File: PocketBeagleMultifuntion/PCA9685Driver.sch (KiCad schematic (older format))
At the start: 18 parts, among them P601 A7 A6 A5 A4 A3 A2 A1 A0 C, P602 B7 B6 B5 B4 B3 B2 B1 B0 C, T601 + 12V -, U601 PCA9685, U602 TBD62X83A, U603 TBD62X83A

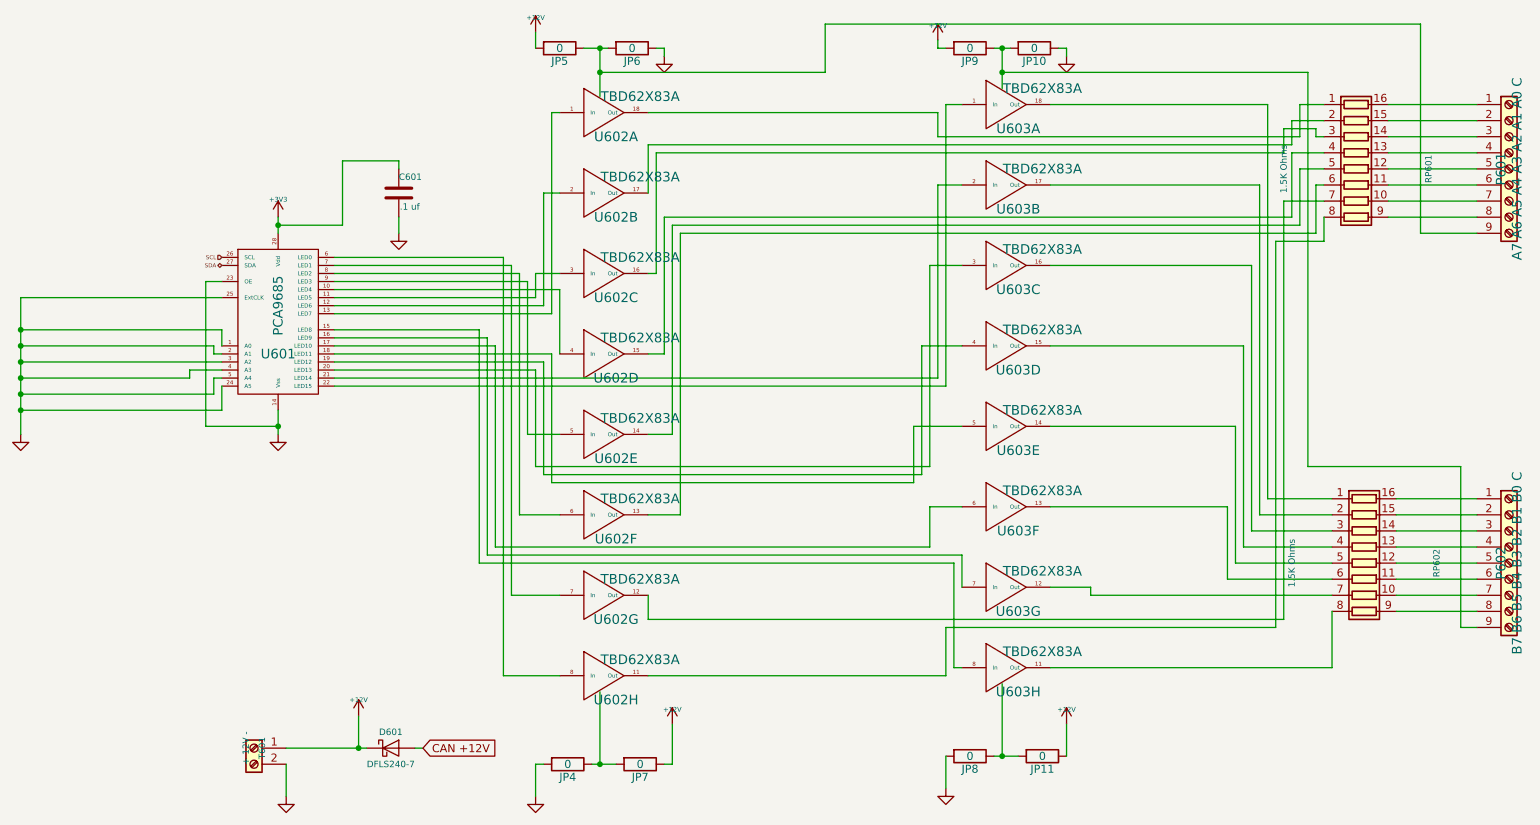
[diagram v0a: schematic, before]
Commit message: PocketBeagleMultifunction completed.
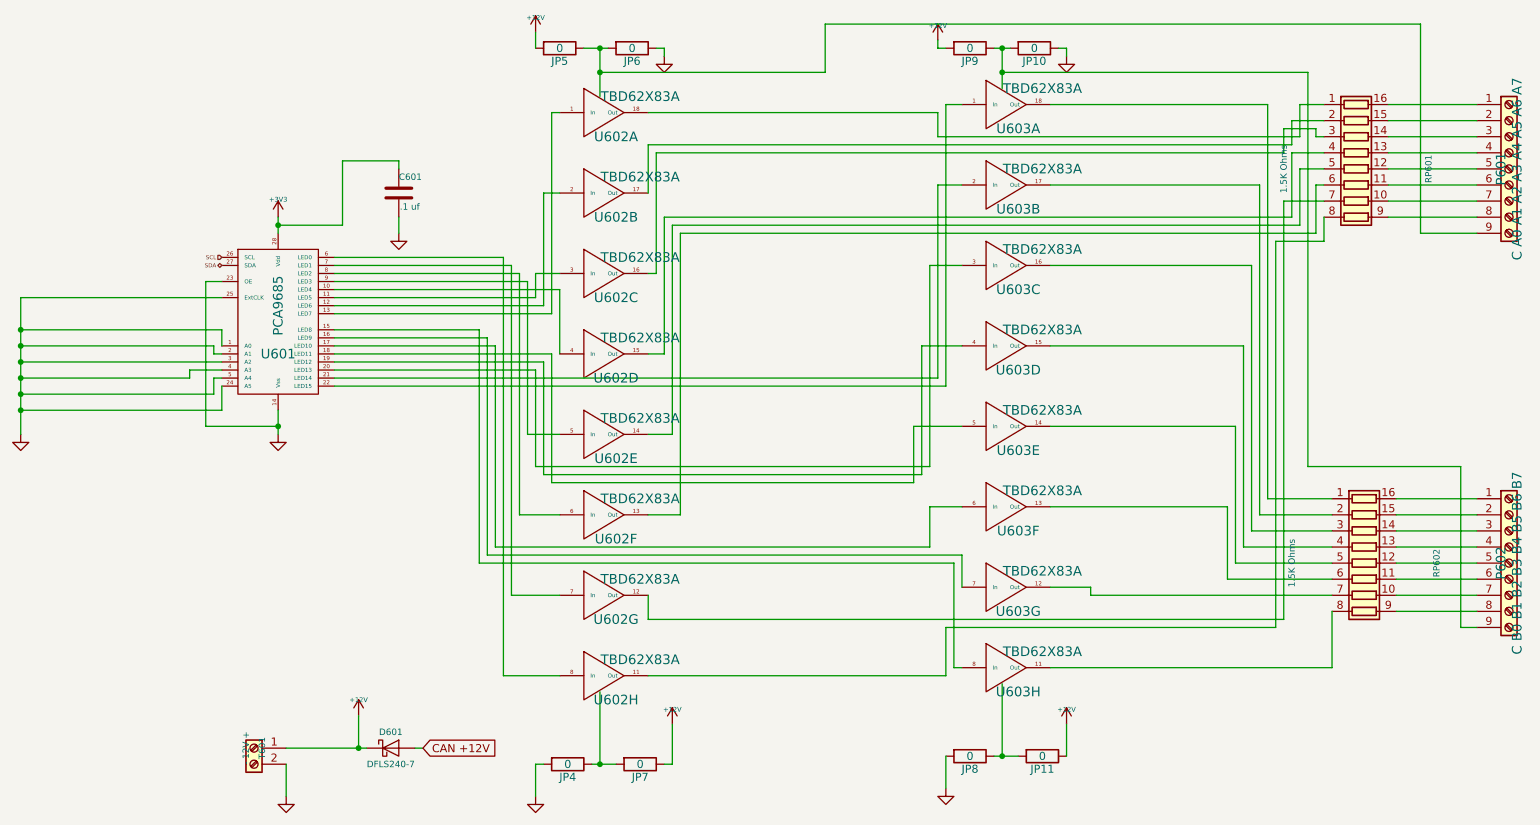
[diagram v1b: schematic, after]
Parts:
- P601: value A7 A6 A5 A4 A3 A2 A1 A0 C -> C A0 A1 A2 A3 A4 A5 A6 A7
- P602: value B7 B6 B5 B4 B3 B2 B1 B0 C -> C B0 B1 B2 B3 B4 B5 B6 B7
- T601: value + 12V - -> - 12V +
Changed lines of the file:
@@
 SDA
 $Comp
-L +3V3 #PWR012
+L +3V3 #PWR016
 U 1 1 5E35C9FF
 P 2800 1750
-F 0 "#PWR012" H 2800 1710 30  0001 C CNN
+F 0 "#PWR016" H 2800 1710 30  0001 C CNN
 F 1 "+3V3" H 2800 1860 30  0000 C CNN
 F 2 "" H 2800 1750 60  0000 C CNN
@@
 $EndComp
 $Comp
-L GND #PWR013
+L GND #PWR017
 U 1 1 5E35CA00
 P 2800 3100
-F 0 "#PWR013" H 2800 3100 30  0001 C CNN
+F 0 "#PWR017" H 2800 3100 30  0001 C CNN
 F 1 "GND" H 2800 3030 30  0001 C CNN
 F 2 "" H 2800 3100 60  0000 C CNN
@@
 $EndComp
 $Comp
-L GND #PWR014
+L GND #PWR018
 U 1 1 5E35CA02
 P 3550 1850
-F 0 "#PWR014" H 3550 1850 30  0001 C CNN
+F 0 "#PWR018" H 3550 1850 30  0001 C CNN
 F 1 "GND" H 3550 1780 30  0001 C CNN
 F 2 "" H 3550 1850 60  0000 C CNN
@@
 P 10450 1450
 F 0 "P601" V 10400 1450 60  0000 C CNN
-F 1 "A7 A6 A5 A4 A3 A2 A1 A0 C" V 10500 1450 60  0000 C CNN
+F 1 "C A0 A1 A2 A3 A4 A5 A6 A7" V 10500 1450 60  0000 C CNN
 F 2 "Connectors_Terminal_Blocks:TerminalBlock_Pheonix_MPT-2.54mm_9pol" H 10450 1450 60  0001 C CNN
 F 3 "~" H 10450 1450 60  0000 C CNN
@@
 P 10450 3900
 F 0 "P602" V 10400 3900 60  0000 C CNN
-F 1 "B7 B6 B5 B4 B3 B2 B1 B0 C" V 10500 3900 60  0000 C CNN
+F 1 "C B0 B1 B2 B3 B4 B5 B6 B7" V 10500 3900 60  0000 C CNN
 F 2 "Connectors_Terminal_Blocks:TerminalBlock_Pheonix_MPT-2.54mm_9pol" H 10450 3900 60  0001 C CNN
 F 3 "~" H 10450 3900 60  0000 C CNN
@@
 $EndComp
 $Comp
-L +12V #PWR015
+L +12V #PWR019
 U 1 1 5E35CA1B
 P 4400 600
-F 0 "#PWR015" H 4400 690 20  0001 C CNN
+F 0 "#PWR019" H 4400 690 20  0001 C CNN
 F 1 "+12V" H 4400 690 30  0000 C CNN
 F 2 "" H 4400 600 60  0000 C CNN
@@
 $EndComp
 $Comp
-L +12V #PWR016
+L +12V #PWR020
 U 1 1 5E35CA1C
 P 6900 650
-F 0 "#PWR016" H 6900 740 20  0001 C CNN
+F 0 "#PWR020" H 6900 740 20  0001 C CNN
 F 1 "+12V" H 6900 740 30  0000 C CNN
 F 2 "" H 6900 650 60  0000 C CNN
@@
 $EndComp
 $Comp
-L +12V #PWR017
+L +12V #PWR021
 U 1 1 5E35CA1D
 P 7700 4900
-F 0 "#PWR017" H 7700 4990 20  0001 C CNN
+F 0 "#PWR021" H 7700 4990 20  0001 C CNN
 F 1 "+12V" H 7700 4990 30  0000 C CNN
 F 2 "" H 7700 4900 60  0000 C CNN
@@
 $EndComp
 $Comp
-L +12V #PWR018
+L +12V #PWR022
 U 1 1 5E35CA1E
 P 5250 4900
-F 0 "#PWR018" H 5250 4990 20  0001 C CNN
+F 0 "#PWR022" H 5250 4990 20  0001 C CNN
 F 1 "+12V" H 5250 4990 30  0000 C CNN
 F 2 "" H 5250 4900 60  0000 C CNN
@@
 $EndComp
 $Comp
-L GND #PWR019
+L GND #PWR023
 U 1 1 5E35CA1F
 P 4400 5350
-F 0 "#PWR019" H 4400 5350 30  0001 C CNN
+F 0 "#PWR023" H 4400 5350 30  0001 C CNN
 F 1 "GND" H 4400 5280 30  0001 C CNN
 F 2 "" H 4400 5350 60  0000 C CNN
@@
 $EndComp
 $Comp
-L GND #PWR020
+L GND #PWR024
 U 1 1 5E35CA20
 P 6950 5300
-F 0 "#PWR020" H 6950 5300 30  0001 C CNN
+F 0 "#PWR024" H 6950 5300 30  0001 C CNN
 F 1 "GND" H 6950 5230 30  0001 C CNN
 F 2 "" H 6950 5300 60  0000 C CNN
@@
 $EndComp
 $Comp
-L GND #PWR021
+L GND #PWR025
 U 1 1 5E35CA21
 P 7700 750
-F 0 "#PWR021" H 7700 750 30  0001 C CNN
+F 0 "#PWR025" H 7700 750 30  0001 C CNN
 F 1 "GND" H 7700 680 30  0001 C CNN
 F 2 "" H 7700 750 60  0000 C CNN
@@
 $EndComp
 $Comp
-L GND #PWR022
+L GND #PWR026
 U 1 1 5E35CA22
 P 5200 750
-F 0 "#PWR022" H 5200 750 30  0001 C CNN
+F 0 "#PWR026" H 5200 750 30  0001 C CNN
 F 1 "GND" H 5200 680 30  0001 C CNN
 F 2 "" H 5200 750 60  0000 C CNN
@@
 $EndComp
 $Comp
-L GND #PWR023
+L GND #PWR027
 U 1 1 5E35CA24
 P 1200 3100
-F 0 "#PWR023" H 1200 3100 30  0001 C CNN
+F 0 "#PWR027" H 1200 3100 30  0001 C CNN
 F 1 "GND" H 1200 3030 30  0001 C CNN
 F 2 "" H 1200 3100 60  0000 C CNN
@@
 $EndComp
 $Comp
-L +12V #PWR024
+L +12V #PWR028
 U 1 1 5E35CA29
 P 3300 4850
-F 0 "#PWR024" H 3300 4800 20  0001 C CNN
+F 0 "#PWR028" H 3300 4800 20  0001 C CNN
 F 1 "+12V" H 3300 4950 30  0000 C CNN
 F 2 "" H 3300 4850 60  0000 C CNN
@@
 P 2650 5050
 F 0 "T601" V 2600 5050 40  0000 C CNN
-F 1 "+ 12V -" V 2700 5050 40  0000 C CNN
+F 1 "- 12V +" V 2700 5050 40  0000 C CNN
 F 2 "Connectors_Terminal_Blocks:TerminalBlock_Pheonix_MPT-2.54mm_2pol" H 2650 5050 60  0001 C CNN
 F 3 "~" H 2650 5050 60  0000 C CNN
@@
 	2850 5050 3350 5050
 $Comp
-L GND #PWR025
+L GND #PWR029
 U 1 1 5E35CA2B
 P 2850 5350
-F 0 "#PWR025" H 2850 5350 30  0001 C CNN
+F 0 "#PWR029" H 2850 5350 30  0001 C CNN
 F 1 "GND" H 2850 5280 30  0001 C CNN
 F 2 "" H 2850 5350 60  0000 C CNN
